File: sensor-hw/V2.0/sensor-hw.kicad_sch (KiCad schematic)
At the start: 0 parts

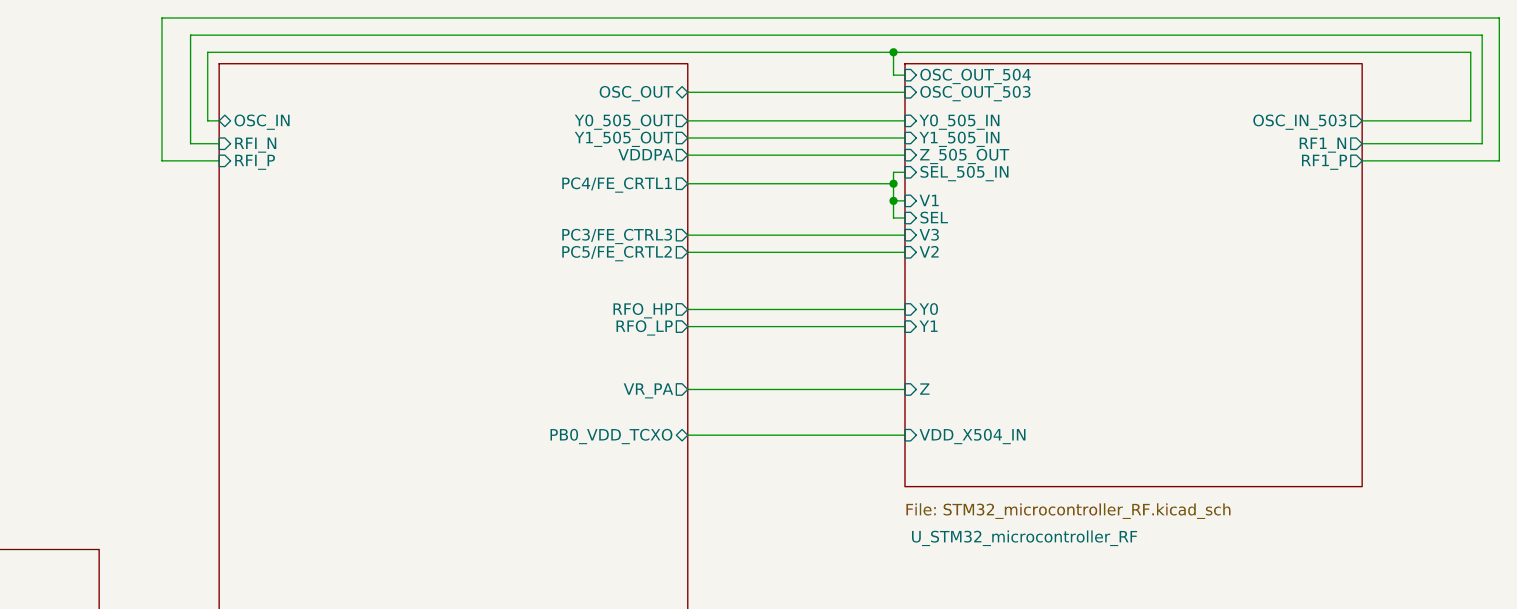
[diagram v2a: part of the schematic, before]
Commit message: updated components fields and footprint in MCU page
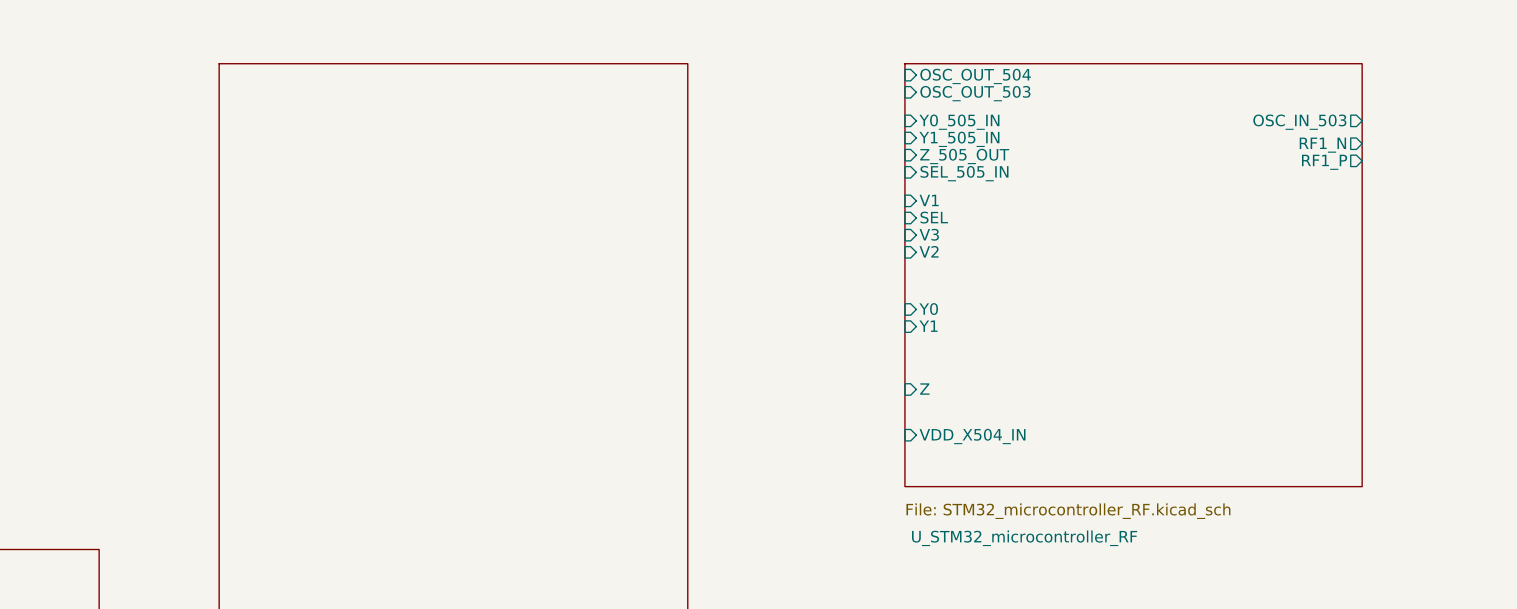
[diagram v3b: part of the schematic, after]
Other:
- sheet STM32WL55xx ports: added none; removed OSC_IN, OSC_OUT, PB0_VDD_TCXO, PC3/FE_CTRL3, PC4/FE_CRTL1, PC5/FE_CRTL2, RFI_N, RFI_P, RFO_HP, RFO_LP, VDDPA, VR_PA, Y0_505_OUT, Y1_505_OUT
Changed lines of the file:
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@@
 (kicad_sch (version 20230121) (generator eeschema)
   (paper "A4")
-  (junction (at 211.455 67.31) (diameter 0) (color 0 0 0 0)
-  )
-  (junction (at 211.455 50.8) (diameter 0) (color 0 0 0 0)
-  )
-  (junction (at 211.455 65.405) (diameter 0) (color 0 0 0 0)
-  )
-  (wire (pts (xy 276.86 60.96) (xy 276.86 48.895))
-    (stroke (width 0) (type default))
-  )
-  (wire (pts (xy 211.455 69.215) (xy 212.725 69.215))
-    (stroke (width 0) (type default))
-  )
-  (wire (pts (xy 188.595 55.245) (xy 212.725 55.245))
-    (stroke (width 0) (type default))
-  )
-  (wire (pts (xy 188.595 71.12) (xy 212.725 71.12))
-    (stroke (width 0) (type default))
-  )
-  (wire (pts (xy 188.595 79.375) (xy 212.725 79.375))
-    (stroke (width 0) (type default))
-  )
-  (wire (pts (xy 212.725 53.34) (xy 211.455 53.34))
-    (stroke (width 0) (type default))
-  )
-  (wire (pts (xy 211.455 67.31) (xy 212.725 67.31))
-    (stroke (width 0) (type default))
-  )
-  (wire (pts (xy 188.595 88.265) (xy 212.725 88.265))
-    (stroke (width 0) (type default))
-  )
   (wire (pts (xy 123.19 115.57) (xy 136.525 115.57))
-    (stroke (width 0) (type default))
-  )
-  (wire (pts (xy 188.595 58.42) (xy 212.725 58.42))
-    (stroke (width 0) (type default))
-  )
-  (wire (pts (xy 211.455 53.34) (xy 211.455 50.8))
-    (stroke (width 0) (type default))
-  )
-  (wire (pts (xy 188.595 60.325) (xy 212.725 60.325))
-    (stroke (width 0) (type default))
-  )
-  (wire (pts (xy 130.175 62.865) (xy 136.525 62.865))
-    (stroke (width 0) (type default))
-  )
-  (wire (pts (xy 211.455 65.405) (xy 211.455 67.31))
-    (stroke (width 0) (type default))
-  )
-  (wire (pts (xy 135.255 58.42) (xy 135.255 50.8))
-    (stroke (width 0) (type default))
-  )
-  (wire (pts (xy 188.595 73.025) (xy 212.725 73.025))
     (stroke (width 0) (type default))
   )
@@
     (stroke (width 0) (type default))
   )
-  (wire (pts (xy 135.255 50.8) (xy 211.455 50.8))
-    (stroke (width 0) (type default))
-  )
-  (wire (pts (xy 278.765 62.865) (xy 278.765 46.99))
-    (stroke (width 0) (type default))
-  )
-  (wire (pts (xy 188.595 62.23) (xy 212.725 62.23))
-    (stroke (width 0) (type default))
-  )
-  (wire (pts (xy 188.595 81.28) (xy 212.725 81.28))
-    (stroke (width 0) (type default))
-  )
-  (wire (pts (xy 263.525 62.865) (xy 278.765 62.865))
-    (stroke (width 0) (type default))
-  )
-  (wire (pts (xy 188.595 65.405) (xy 211.455 65.405))
-    (stroke (width 0) (type default))
-  )
   (wire (pts (xy 123.19 125.73) (xy 136.525 125.73))
-    (stroke (width 0) (type default))
-  )
-  (wire (pts (xy 263.525 60.96) (xy 276.86 60.96))
-    (stroke (width 0) (type default))
-  )
-  (wire (pts (xy 133.35 48.895) (xy 133.35 60.96))
-    (stroke (width 0) (type default))
-  )
-  (wire (pts (xy 263.525 58.42) (xy 275.59 58.42))
-    (stroke (width 0) (type default))
-  )
-  (wire (pts (xy 211.455 50.8) (xy 275.59 50.8))
-    (stroke (width 0) (type default))
-  )
-  (wire (pts (xy 278.765 46.99) (xy 130.175 46.99))
-    (stroke (width 0) (type default))
-  )
-  (wire (pts (xy 188.595 93.345) (xy 212.725 93.345))
-    (stroke (width 0) (type default))
-  )
-  (wire (pts (xy 276.86 48.895) (xy 133.35 48.895))
-    (stroke (width 0) (type default))
-  )
-  (wire (pts (xy 130.175 46.99) (xy 130.175 62.865))
-    (stroke (width 0) (type default))
-  )
-  (wire (pts (xy 136.525 58.42) (xy 135.255 58.42))
-    (stroke (width 0) (type default))
-  )
-  (wire (pts (xy 211.455 65.405) (xy 211.455 64.135))
-    (stroke (width 0) (type default))
-  )
-  (wire (pts (xy 275.59 50.8) (xy 275.59 58.42))
-    (stroke (width 0) (type default))
-  )
-  (wire (pts (xy 211.455 67.31) (xy 211.455 69.215))
-    (stroke (width 0) (type default))
-  )
-  (wire (pts (xy 211.455 64.135) (xy 212.725 64.135))
-    (stroke (width 0) (type default))
-  )
-  (wire (pts (xy 133.35 60.96) (xy 136.525 60.96))
     (stroke (width 0) (type default))
   )
@@
       (effects (font (size 1.27 1.27)) (justify left top))
     )
-    (pin "Y1_505_OUT" output (at 188.595 60.325 0)
-      (effects (font (size 1.27 1.27)) (justify right))
-    )
-    (pin "PC3{slash}FE_CTRL3" output (at 188.595 71.12 0)
-      (effects (font (size 1.27 1.27)) (justify right))
-    )
-    (pin "PC4{slash}FE_CRTL1" output (at 188.595 65.405 0)
-      (effects (font (size 1.27 1.27)) (justify right))
-    )
-    (pin "PC5{slash}FE_CRTL2" output (at 188.595 73.025 0)
-      (effects (font (size 1.27 1.27)) (justify right))
-    )
-    (pin "VDDPA" output (at 188.595 62.23 0)
-      (effects (font (size 1.27 1.27)) (justify right))
-    )
-    (pin "RFI_P" input (at 136.525 62.865 180)
-      (effects (font (size 1.27 1.27)) (justify left))
-    )
-    (pin "RFO_LP" output (at 188.595 81.28 0)
-      (effects (font (size 1.27 1.27)) (justify right))
-    )
-    (pin "OSC_OUT" bidirectional (at 188.595 55.245 0)
-      (effects (font (size 1.27 1.27)) (justify right))
-    )
-    (pin "OSC_IN" bidirectional (at 136.525 58.42 180)
-      (effects (font (size 1.27 1.27)) (justify left))
-    )
-    (pin "VR_PA" output (at 188.595 88.265 0)
-      (effects (font (size 1.27 1.27)) (justify right))
-    )
-    (pin "Y0_505_OUT" output (at 188.595 58.42 0)
-      (effects (font (size 1.27 1.27)) (justify right))
-    )
-    (pin "RFI_N" input (at 136.525 60.96 180)
-      (effects (font (size 1.27 1.27)) (justify left))
-    )
-    (pin "RFO_HP" output (at 188.595 79.375 0)
-      (effects (font (size 1.27 1.27)) (justify right))
-    )
-    (pin "PB0_VDD_TCXO" bidirectional (at 188.595 93.345 0)
-      (effects (font (size 1.27 1.27)) (justify right))
-    )
     (pin "VDD" input (at 136.525 125.73 180)
